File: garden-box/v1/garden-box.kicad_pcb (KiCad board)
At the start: 2 copper layers, 88.9 x 66 mm, 28 parts, among them J1 Conn_01x05_Male, J2 Screw_Terminal_01x02, J3 Screw_Terminal_01x02, J4 Screw_Terminal_01x02, Q1 IRF830, Q2 BT136-600, U1 4N35, U2 H11AA1, U3 MOC3021M

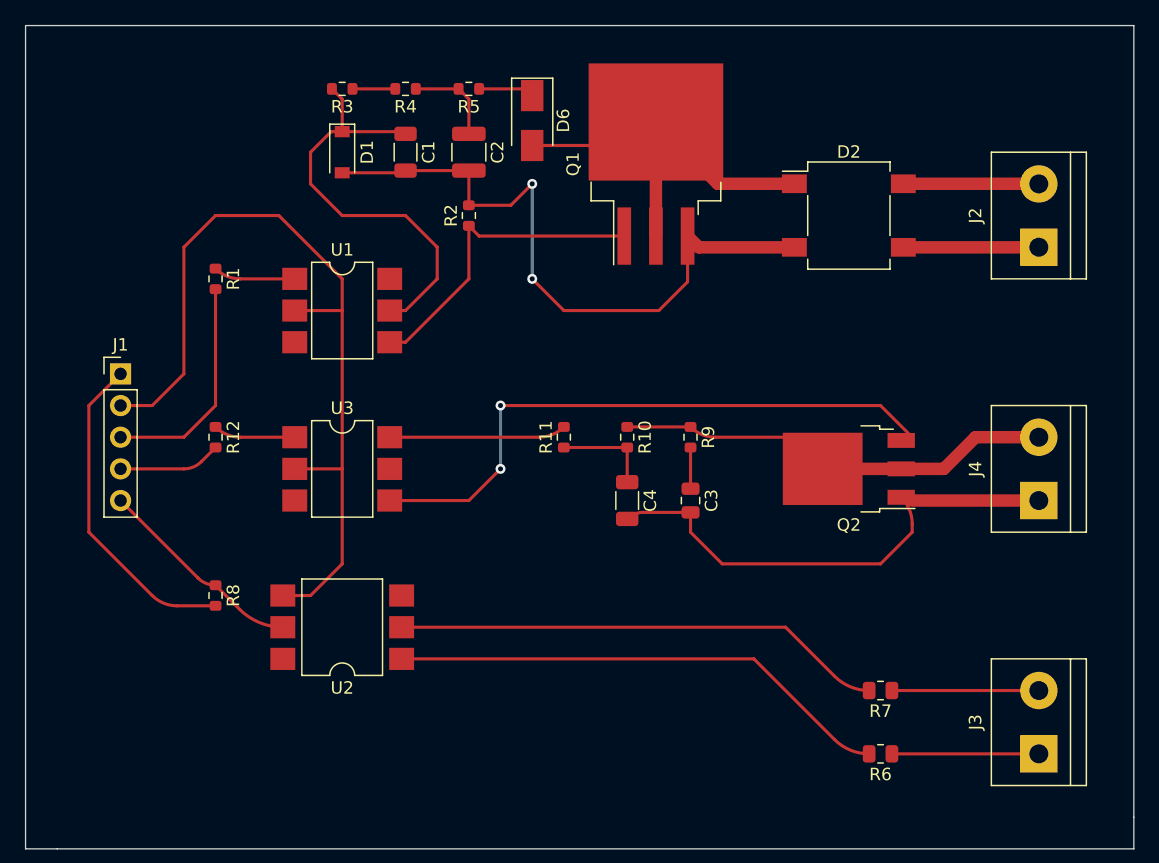
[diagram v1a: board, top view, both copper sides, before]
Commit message: add relay footprints
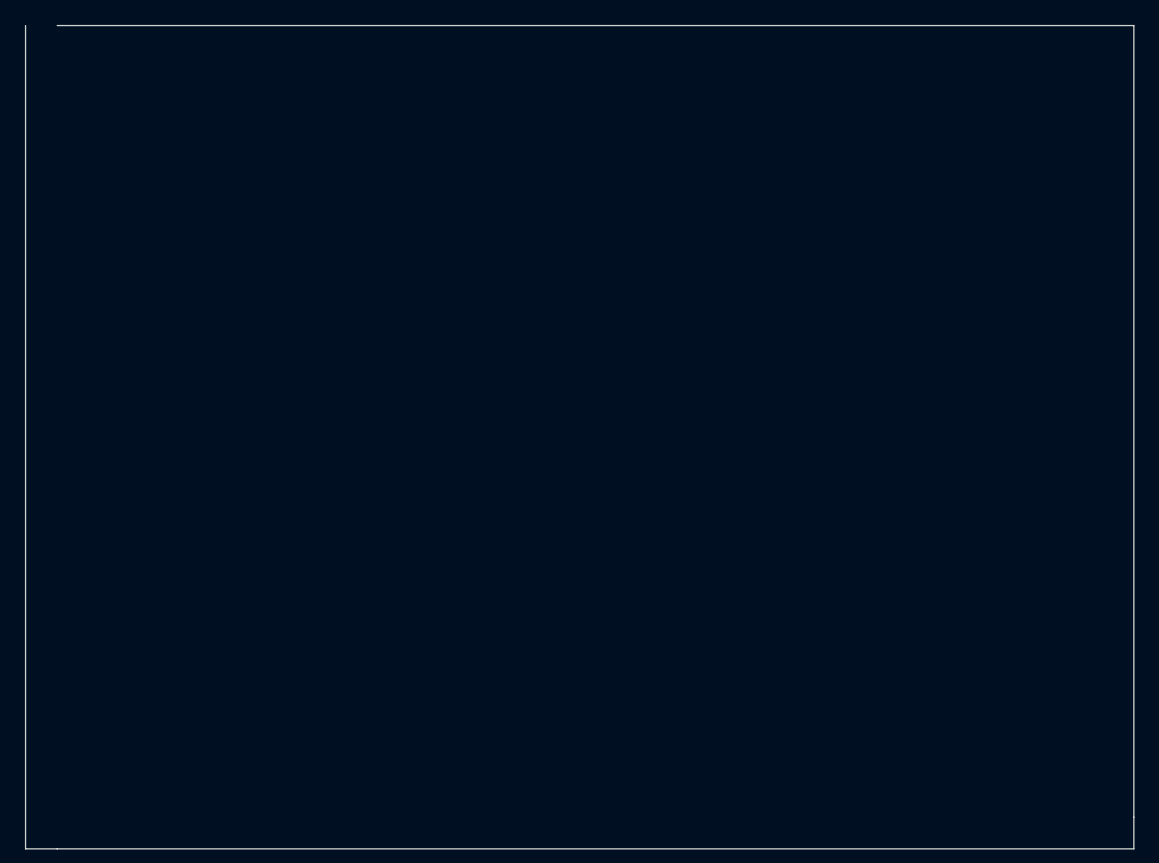
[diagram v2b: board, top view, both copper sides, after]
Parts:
- removed C1: 2.2uF/63V, Capacitor_SMD:C_1206_3216Metric
- removed C2: 220nF/275V, Capacitor_SMD:C_1210_3225Metric
- removed C3: 10nF, Capacitor_SMD:C_0805_2012Metric
- removed C4: 47nF, Capacitor_SMD:C_1206_3216Metric
- removed D1: 10V/0.4W, Diode_SMD:D_SOD-123
- removed D2: 4* 1N5408, Diode_SMD:Diode_Bridge_Diotec_SO-DIL-Slim
- removed D6: 1N4007, Diode_SMD:D_SMA
- removed J1: Conn_01x05_Male, Connector_PinHeader_2.54mm:PinHeader_1x05_P2.54mm_Vertical
- removed J2, J3, J4: Screw_Terminal_01x02, TerminalBlock:TerminalBlock_bornier-2_P5.08mm
- removed Q1: IRF830, Package_TO_SOT_SMD:TO-263-3_TabPin2
- removed Q2: BT136-600, Package_TO_SOT_SMD:TO-252-3_TabPin2
- removed R1: 330Ω, Resistor_SMD:R_0603_1608Metric
- removed R10: 470Ω, Resistor_SMD:R_0603_1608Metric
- removed R11: 360Ω, Resistor_SMD:R_0603_1608Metric
- removed R12, R5: 220Ω, Resistor_SMD:R_0603_1608Metric
- removed R2: 22KΩ, Resistor_SMD:R_0603_1608Metric
- removed R3, R4: 33KΩ, Resistor_SMD:R_0603_1608Metric
- removed R6, R7: 33KΩ/0.5W, Resistor_SMD:R_0805_2012Metric
- removed R8: 10KΩ, Resistor_SMD:R_0603_1608Metric
- removed R9: 39Ω, Resistor_SMD:R_0603_1608Metric
- removed U1: 4N35, Package_DIP:SMDIP-6_W7.62mm
- removed U2: H11AA1, Package_DIP:SMDIP-6_W9.53mm
- removed U3: MOC3021M, Package_DIP:SMDIP-6_W7.62mm
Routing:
- net GND: track 68.4 -> 0.00 mm
- net Net-(C1-Pad2): track 53.5 -> 0.00 mm, vias 2 -> 0
- net Net-(Q2-Pad3): track 50.0 -> 0.00 mm, vias 2 -> 0
- net Net-(C3-Pad2): track 40.8 -> 0.00 mm
- net Net-(R6-Pad2): track 40.5 -> 0.00 mm
- net Net-(R7-Pad2): track 39.4 -> 0.00 mm
- net Net-(Q2-Pad2): track 35.3 -> 0.00 mm
- net Net-(C1-Pad1): track 34.4 -> 0.00 mm
- net Net-(D2-Pad1): track 33.0 -> 0.00 mm
- net +3V3: track 26.2 -> 0.00 mm
- net Net-(Q1-Pad1): track 25.5 -> 0.00 mm
- net Net-(J1-Pad3): track 18.0 -> 0.00 mm
- net Net-(J1-Pad5): track 17.3 -> 0.00 mm
- net Net-(R11-Pad2): track 14.2 -> 0.00 mm
- net Net-(J3-Pad2): track 11.8 -> 0.00 mm
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
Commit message: init new v1
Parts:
- added D1: LED, Diode_SMD:D_0805_2012Metric, F.Cu at (198.5, 128.9)
- added D2: 1N4148, Diode_SMD:D_SOD-123, F.Cu at (202.3, 129.5)
- added J1: USB_A, rs-online:875200010BLF, F.Cu at (52.4, 95.0)
- added J2: Conn_01x03_Male, Connector_PinHeader_2.54mm:PinHeader_1x03_P2.54mm_Vertical, F.Cu at (162.6, 49.5)
- added J3: Conn_01x04_Male, Connector_PinHeader_2.54mm:PinHeader_1x04_P2.54mm_Vertical, F.Cu at (152.4, 49.5)
- added J4: Screw_Terminal_01x02, TerminalBlock:TerminalBlock_bornier-2_P5.08mm, F.Cu at (185.8, 151.1)
- added J5: Screw_Terminal_01x02, TerminalBlock:TerminalBlock_bornier-2_P5.08mm, F.Cu at (205.5, 151.1)
- added J6: Screw_Terminal_01x02, TerminalBlock:TerminalBlock_bornier-2_P5.08mm, F.Cu at (223.9, 151.1)
- added K1: G6DN-1A-L_DC5, rs-online:G6DN-1A-L, F.Cu at (228.0, 127.0)
- added PS1: RS PRO 5V 2A, mylife-footprints:RS PRO 5V 2A, F.Cu at (73.3, 74.3)
- added Q1: 2N3904, jlcpcb:SOT-23-3_L2.9-W1.3-P1.90-LS2.4-TR, F.Cu at (194.0, 130.8)
- added R1: 4.7KΩ, Resistor_SMD:R_0402_1005Metric, F.Cu at (157.5, 53.3)
- added R2: 1KΩ, Resistor_SMD:R_0402_1005Metric, F.Cu at (195.6, 127.6)
- added R3: 10KΩ, Resistor_SMD:R_0402_1005Metric, F.Cu at (192.8, 127.6)
- added R4: 330Ω, Resistor_SMD:R_0402_1005Metric, F.Cu at (198.5, 132.1)
- added REF**: MountingHole_3.2mm_M3_Pad_Via, MountingHole:MountingHole_3.2mm_M3_Pad_Via, F.Cu at (245.9, 159.2)
- added REF**: MountingHole_3.2mm_M3_Pad_Via, MountingHole:MountingHole_3.2mm_M3_Pad_Via, F.Cu at (44.5, 159.2)
- added REF**: MountingHole_3.2mm_M3_Pad_Via, MountingHole:MountingHole_3.2mm_M3_Pad_Via, F.Cu at (44.5, 21.2)
- added REF**: MountingHole_3.2mm_M3_Pad_Via, MountingHole:MountingHole_3.2mm_M3_Pad_Via, F.Cu at (37.2, 90.2)
- added REF**: MountingHole_3.2mm_M3_Pad_Via, MountingHole:MountingHole_3.2mm_M3_Pad_Via, F.Cu at (253.2, 90.2)
- added REF**: MountingHole_4.3mm_M4, MountingHole:MountingHole_4.3mm_M4, F.Cu at (143.6, 84.7)
- added REF**: MountingHole_4.3mm_M4, MountingHole:MountingHole_4.3mm_M4, F.Cu at (49.6, 84.7)
- added REF**: MountingHole_3.2mm_M3_Pad_Via, MountingHole:MountingHole_3.2mm_M3_Pad_Via, F.Cu at (245.9, 21.2)
- added T1: Transformer_1P_2S, rs-online:VCM36212, F.Cu at (191.4, 79.1)
- added U1: ESP32-POE, mylife-footprints:ESP32-POE, F.Cu at (84.5, 40.6)
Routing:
- net Net-(J4-Pad2): track 0.00 -> 347.0 mm
- net GND: track 0.00 -> 282.4 mm
- net +5V: track 0.00 -> 266.7 mm, vias 0 -> 1
- net Net-(R2-Pad2): track 0.00 -> 198.1 mm
- net Net-(J4-Pad1): track 0.00 -> 196.1 mm
- net Net-(J6-Pad1): track 0.00 -> 116.8 mm
- net Net-(J3-Pad4): track 0.00 -> 110.3 mm
- net Net-(J5-Pad1): track 0.00 -> 99.8 mm
- net +3V3: track 0.00 -> 96.6 mm, vias 0 -> 1
- net Net-(J2-Pad3): track 0.00 -> 92.0 mm
- net Net-(J6-Pad2): track 0.00 -> 84.3 mm
- net Net-(D1-Pad1): track 0.00 -> 25.3 mm
- net Net-(T1-Pad4): track 0.00 -> 20.0 mm
- net Net-(Q1-Pad2): track 0.00 -> 3.74 mm
- net Net-(D1-Pad2): track 0.00 -> 2.45 mm
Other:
- board size 88.9 x 66 mm -> 230 x 150 mm
- board text added: "220V IN"
- board text added: "220V OUT"
- board text added: "24V~ OUT"
- board text added: "3V3"
- board text added: "5V"
- board text added: "A0"
- board text added: "DS18B20"
- board text added: "GND"
- board text added: "IN"
- board text added: "L"
- board text added: "N"
- board text added: "SEN0308"
- board text added: "SWITCH"

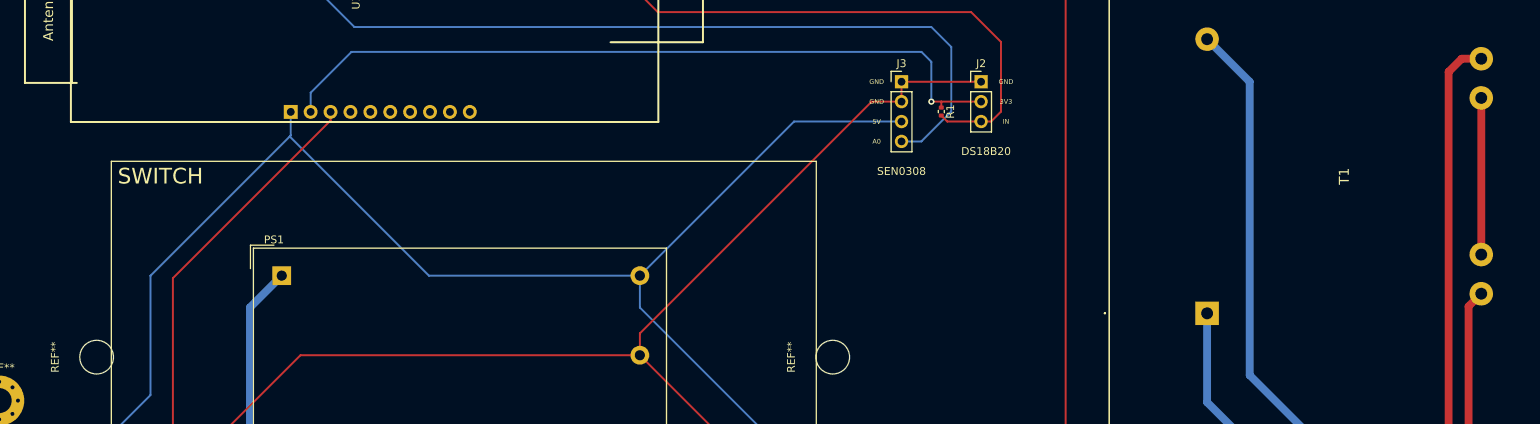
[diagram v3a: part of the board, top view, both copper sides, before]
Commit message: update footprint on PCB
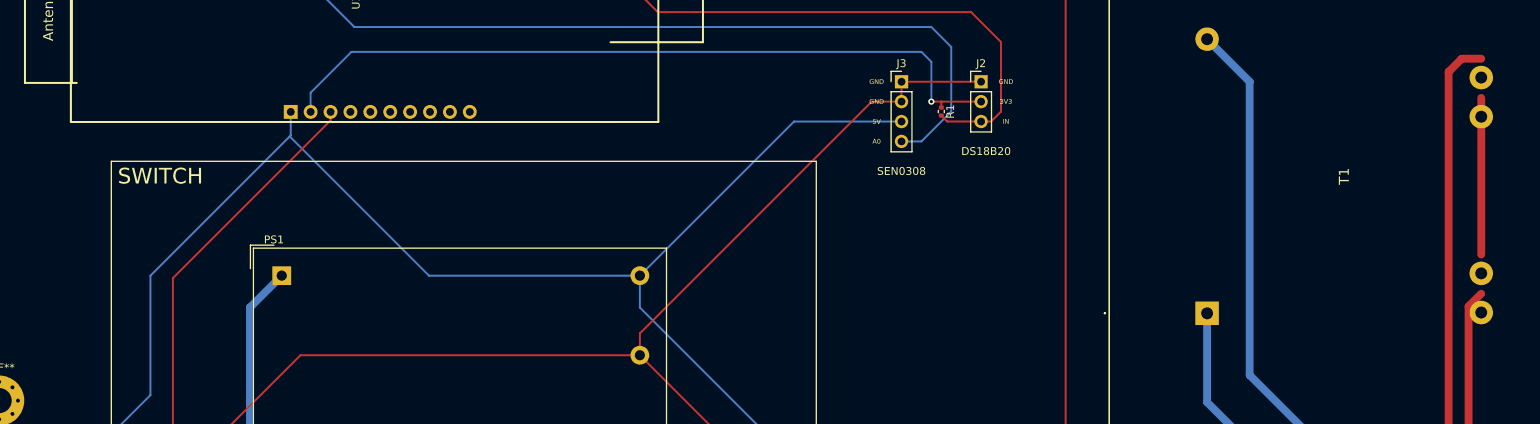
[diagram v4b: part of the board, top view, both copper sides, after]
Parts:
- removed the REF** at (143.6, 84.7)
- removed the REF** at (49.6, 84.7)
- R4: value 330Ω -> 1KΩ
- T1: footprint rs-online:VCM36212 -> mylife-footprints:VCM36212
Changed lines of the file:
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@@
     (descr "Resistor SMD 0402 (1005 Metric), square (rectangular) end terminal, IPC_7351 nominal, (Body size source: IPC-SM-782 page 72, https://www.pcb-3d.com/wordpress/wp-content/uploads/ipc-sm-782a_amendment_1_and_2.pdf), generated with kicad-footprint-generator")
     (tags "resistor")
-    (property "LCSC" "C25104")
+    (property "LCSC" "C11702")
     (property "Sheetfile" "garden-box.kicad_sch")
     (property "Sheetname" "")
@@
       (effects (font (size 1 1) (thickness 0.15)))
     )
-    (fp_text value "330Ω" (at 0 1.17) (layer "F.Fab")
+    (fp_text value "1KΩ" (at 0 1.17) (layer "F.Fab")
       (effects (font (size 1 1) (thickness 0.15)))
     )
@@
     )
   )
-  (footprint "rs-online:VCM36212" (layer "F.Cu")
+  (footprint "mylife-footprints:VCM36212" (layer "F.Cu")
     (at 191.415 79.095 90)
     (descr "VCM 36/2/12")
@@
       (effects (font (size 1.27 1.27) (thickness 0.254)))
     )
+    (fp_line (start -26.1 -12.5) (end -26.1 47.5) (layer "F.SilkS") (width 0.2))
     (fp_line (start 0 -13) (end 0 -13) (layer "F.SilkS") (width 0.2))
     (fp_line (start 0 -13.1) (end 0 -13.1) (layer "F.SilkS") (width 0.2))
     (fp_line (start -26.1 47.5) (end 61.1 47.5) (layer "F.SilkS") (width 0.2))
+    (fp_line (start 0 -13.1) (end 0 -13.1) (layer "F.SilkS") (width 0.2))
+    (fp_line (start 61.1 47.5) (end 61.1 -12.5) (layer "F.SilkS") (width 0.2))
     (fp_line (start 61.1 -12.5) (end -26.1 -12.5) (layer "F.SilkS") (width 0.2))
-    (fp_line (start 61.1 47.5) (end 61.1 -12.5) (layer "F.SilkS") (width 0.2))
-    (fp_line (start -26.1 -12.5) (end -26.1 47.5) (layer "F.SilkS") (width 0.2))
-    (fp_line (start 0 -13.1) (end 0 -13.1) (layer "F.SilkS") (width 0.2))
     (fp_arc (start 0 -13.1) (mid 0.05 -13.05) (end 0 -13) (layer "F.SilkS") (width 0.2))
     (fp_arc (start 0 -13) (mid -0.05 -13.05) (end 0 -13.1) (layer "F.SilkS") (width 0.2))
     (fp_arc (start 0 -13) (mid -0.05 -13.05) (end 0 -13.1) (layer "F.SilkS") (width 0.2))
     (fp_line (start 62.1 48.5) (end 62.1 -13.5) (layer "F.CrtYd") (width 0.1))
+    (fp_line (start -27.1 -13.5) (end -27.1 48.5) (layer "F.CrtYd") (width 0.1))
     (fp_line (start 62.1 -13.5) (end -27.1 -13.5) (layer "F.CrtYd") (width 0.1))
-    (fp_line (start -27.1 -13.5) (end -27.1 48.5) (layer "F.CrtYd") (width 0.1))
     (fp_line (start -27.1 48.5) (end 62.1 48.5) (layer "F.CrtYd") (width 0.1))
-    (fp_line (start -26.1 -12.5) (end -26.1 47.5) (layer "F.Fab") (width 0.1))
-    (fp_line (start -26.1 47.5) (end 61.1 47.5) (layer "F.Fab") (width 0.1))
     (fp_line (start 61.1 47.5) (end 61.1 -12.5) (layer "F.Fab") (width 0.1))
     (fp_line (start 61.1 -12.5) (end -26.1 -12.5) (layer "F.Fab") (width 0.1))
+    (fp_line (start -26.1 47.5) (end 61.1 47.5) (layer "F.Fab") (width 0.1))
+    (fp_line (start -26.1 -12.5) (end -26.1 47.5) (layer "F.Fab") (width 0.1))
     (pad "1" thru_hole rect (at 0 0 90) (size 3 3) (drill 1.52) (layers *.Cu *.Mask)
       (net 12 "Net-(J5-Pad1)") (pinfunction "AA") (pintype "passive"))
     (pad "2" thru_hole circle (at 35 0 90) (size 3 3) (drill 1.52) (layers *.Cu *.Mask)
       (net 11 "Net-(J4-Pad2)") (pinfunction "AB") (pintype "passive"))
-    (pad "3" thru_hole circle (at 32.5 35 90) (size 3 3) (drill 1.52) (layers *.Cu *.Mask)
+    (pad "3" thru_hole circle (at 30.1 35 90) (size 3 3) (drill 1.52) (layers *.Cu *.Mask)
       (net 13 "Net-(J6-Pad1)") (pinfunction "SA") (pintype "passive"))
-    (pad "4" thru_hole circle (at 27.5 35 90) (size 3 3) (drill 1.52) (layers *.Cu *.Mask)
+    (pad "4" thru_hole circle (at 25.1 35 90) (size 3 3) (drill 1.52) (layers *.Cu *.Mask)
       (net 17 "Net-(T1-Pad4)") (pinfunction "SB") (pintype "passive"))
-    (pad "5" thru_hole circle (at 7.5 35 90) (size 3 3) (drill 1.52) (layers *.Cu *.Mask)
+    (pad "5" thru_hole circle (at 5.1 35 90) (size 3 3) (drill 1.52) (layers *.Cu *.Mask)
       (net 17 "Net-(T1-Pad4)") (pinfunction "SC") (pintype "passive"))
-    (pad "6" thru_hole circle (at 2.5 35 90) (size 3 3) (drill 1.52) (layers *.Cu *.Mask)
+    (pad "6" thru_hole circle (at 0.1 35 90) (size 3 3) (drill 1.52) (layers *.Cu *.Mask)
       (net 14 "Net-(J6-Pad2)") (pinfunction "SD") (pintype "passive"))
     (pad "MH1" thru_hole circle (at -21.25 -6.25 90) (size 6.6 6.6) (drill 4.4) (layers *.Cu *.Mask))
@@
     (pad "1" thru_hole circle locked (at 0 -2.4) (size 0.8 0.8) (drill 0.5) (layers *.Cu *.Mask))
     (pad "1" thru_hole circle locked (at 2.4 0) (size 0.8 0.8) (drill 0.5) (layers *.Cu *.Mask))
-  )
-  (footprint "MountingHole:MountingHole_4.3mm_M4" (layer "F.Cu")
-    (at 143.62 84.69 90)
-    (descr "Mounting Hole 4.3mm, no annular, M4")
-    (tags "mounting hole 4.3mm no annular m4")
-    (attr exclude_from_pos_files exclude_from_bom)
-    (fp_text reference "REF**" (at 0 -5.3 90) (layer "F.SilkS")
-      (effects (font (size 1 1) (thickness 0.15)))
-    )
-    (fp_text value "MountingHole_4.3mm_M4" (at 0 5.3 90) (layer "F.Fab")
-      (effects (font (size 1 1) (thickness 0.15)))
-    )
-    (fp_text user "${REFERENCE}" (at 0.3 0 90) (layer "F.Fab")
-      (effects (font (size 1 1) (thickness 0.15)))
-    )
-    (fp_circle (center 0 0) (end 4.3 0) (layer "Cmts.User") (width 0.15) (fill none))
-    (fp_circle (center 0 0) (end 4.55 0) (layer "F.CrtYd") (width 0.05) (fill none))
-    (pad "" np_thru_hole circle locked (at 0 0 90) (size 4.3 4.3) (drill 4.3) (layers *.Cu *.Mask))
-  )
-  (footprint "MountingHole:MountingHole_4.3mm_M4" (layer "F.Cu")
-    (at 49.64 84.69 90)
-    (descr "Mounting Hole 4.3mm, no annular, M4")
-    (tags "mounting hole 4.3mm no annular m4")
-    (attr exclude_from_pos_files exclude_from_bom)
-    (fp_text reference "REF**" (at 0 -5.3 90) (layer "F.SilkS")
-      (effects (font (size 1 1) (thickness 0.15)))
-    )
-    (fp_text value "MountingHole_4.3mm_M4" (at 0 5.3 90) (layer "F.Fab")
-      (effects (font (size 1 1) (thickness 0.15)))
-    )
-    (fp_text user "${REFERENCE}" (at 0.3 0 90) (layer "F.Fab")
-      (effects (font (size 1 1) (thickness 0.15)))
-    )
-    (fp_circle (center 0 0) (end 4.3 0) (layer "Cmts.User") (width 0.15) (fill none))
-    (fp_circle (center 0 0) (end 4.55 0) (layer "F.CrtYd") (width 0.05) (fill none))
-    (pad "" np_thru_hole circle locked (at 0 0 90) (size 4.3 4.3) (drill 4.3) (layers *.Cu *.Mask))
   )
   (footprint "Resistor_SMD:R_0402_1005Metric" (layer "F.Cu")
@@
       5f781c26-a274-4ed6-bd9f-a8d1a5767cf4
       a48d5c9d-4ac8-4da0-92f0-6fa35676566b
-      be76b0aa-ff8d-42bb-a430-fcd7f8ce8487
-      cbf90f79-9f70-4e7e-8c0f-189777d524c0
-    )
-  )
+    )
+  )
